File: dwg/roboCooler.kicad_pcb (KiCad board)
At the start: 2 copper layers, 61 x 78.7 mm, 66 parts, among them J1 CONN_01X02, J10 CONN_02X03, J11 CONN_01X04, J12 USB_A, J13 CONN_02X03, J14 CONN_02X03, J2 CONN_01X02, J3 Discovery_F407_P1, J4 CONN_01X06, J5 CONN_01X12, J6 Discovery_F407_P2, J7 CONN_02X03, J8 CONN_02X03, Q1 NMOS, Q2 NMOS, U1 SN74LV, U2 TB6549

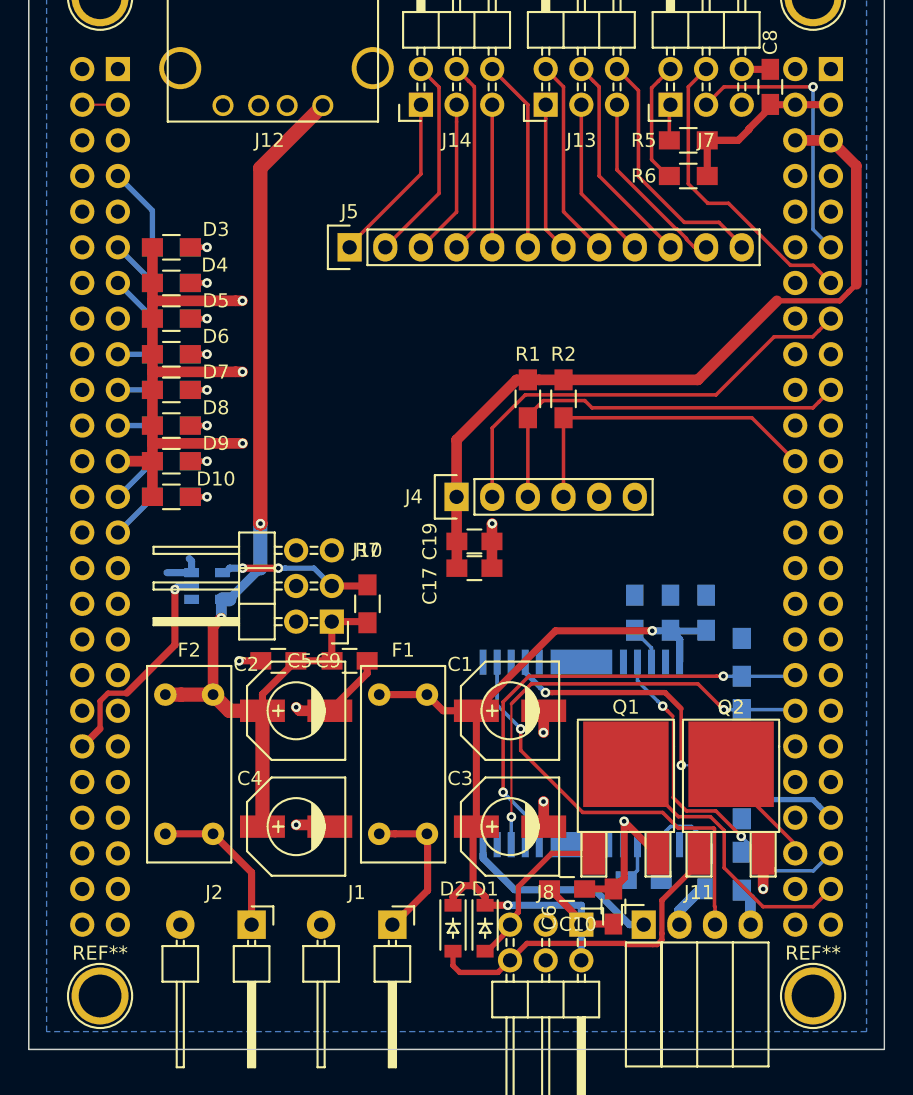
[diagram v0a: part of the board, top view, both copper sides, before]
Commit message: increased trace widths for led driver
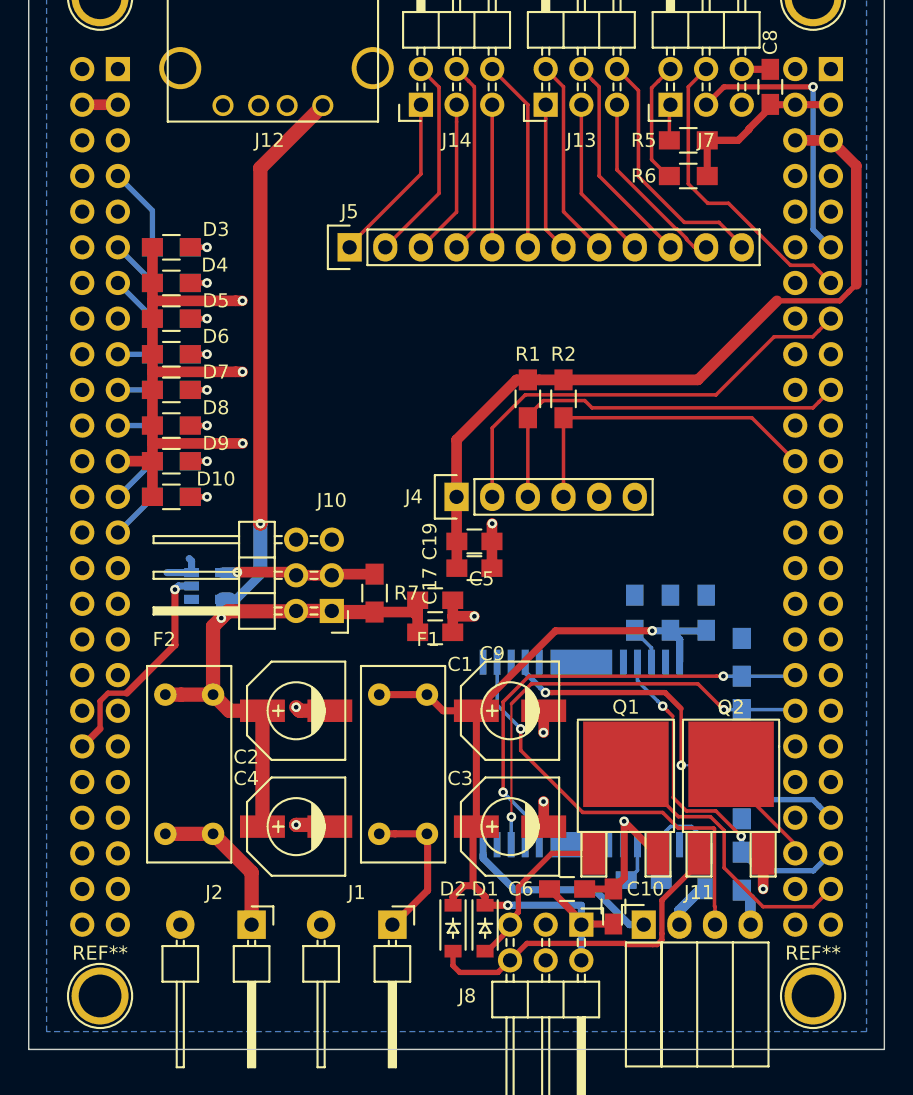
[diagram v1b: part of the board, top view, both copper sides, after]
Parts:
- moved C9 11.4 mm to (50.5, 65.5), turned to 0 degrees
- moved C5 7.47 mm to (50.5, 63.2)
- moved R7 0.92 mm to (46.2, 62.7)
- moved J10 0.76 mm to (43.2, 64.0)
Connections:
- J10 pad 2: (no net) -> +5V
- J10 pad 4: (no net) -> Net-(J10-Pad3)
- J10 pad 6: (no net) -> GND
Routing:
- net +5V: track 73.8 -> 78.6 mm
- net GND: track 81.5 -> 79.2 mm
- net MOTOR_SB: track 24.7 -> 25.3 mm
- net Net-(J10-Pad3): track 11.1 -> 11.0 mm, vias 2 -> 1

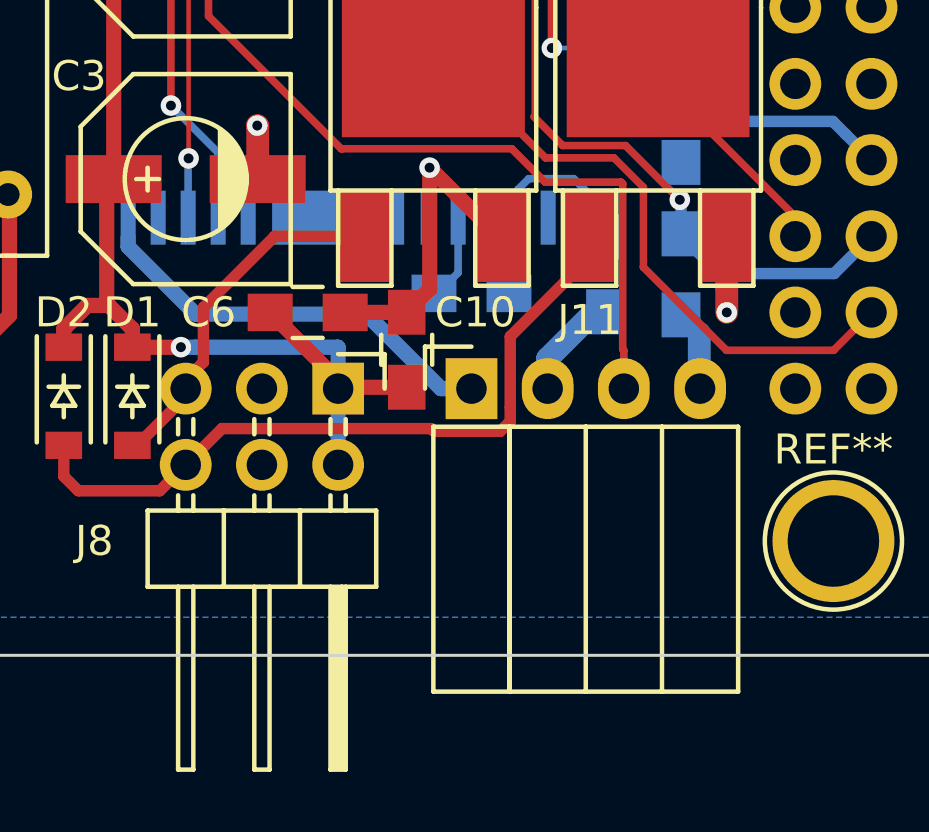
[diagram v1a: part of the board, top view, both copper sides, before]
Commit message: moved J11 to the same 6pin connector.
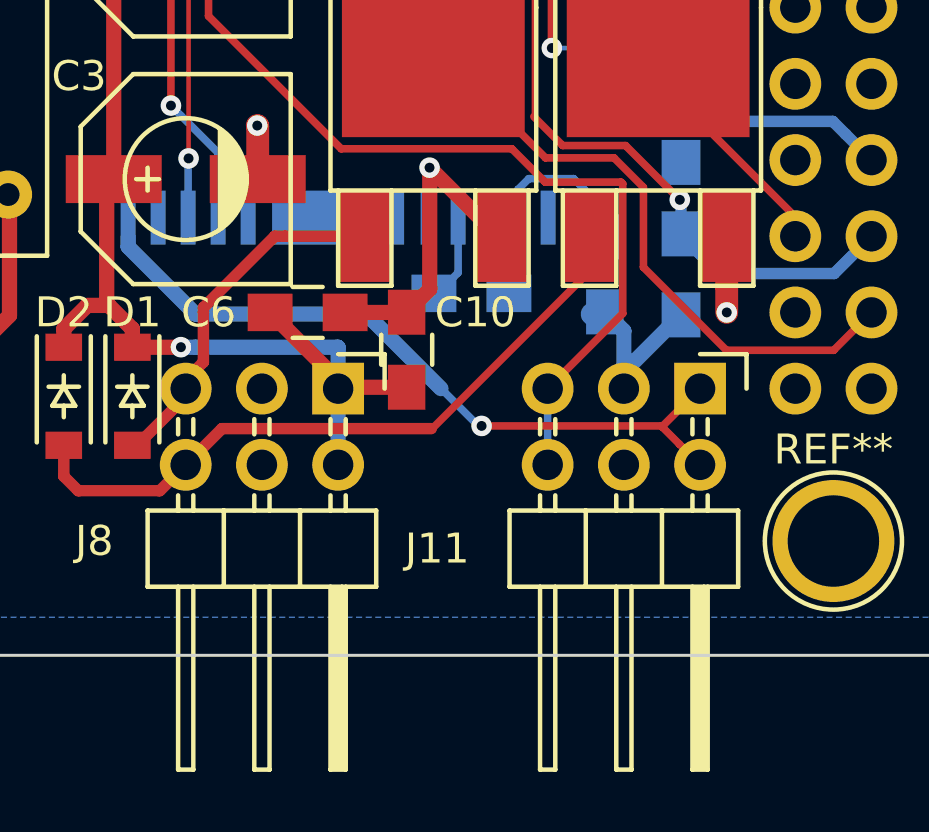
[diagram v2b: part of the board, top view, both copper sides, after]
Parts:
- J11: value CONN_01X04 -> CONN_02X03; footprint Socket_Strips:Socket_Strip_Angled_1x04 -> Pin_Headers:Pin_Header_Angled_2x03
- moved J11 7.62 mm to (73.0, 86.4), turned to 270 degrees
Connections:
- J11 pad 2: GND -> MOTOR_OUT1
- J11 pad 3: MOTOR_OUT2 -> GND
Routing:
- net MOTOR_OUT1: track 14.4 -> 24.9 mm, vias 0 -> 1
- net MOTOR_OUT2: track 30.1 -> 34.1 mm
- net Net-(D2-Pad2): track 24.8 -> 23.3 mm

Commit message: tweaked layout before ordering
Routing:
- net +12V: track 65.7 -> 64.9 mm

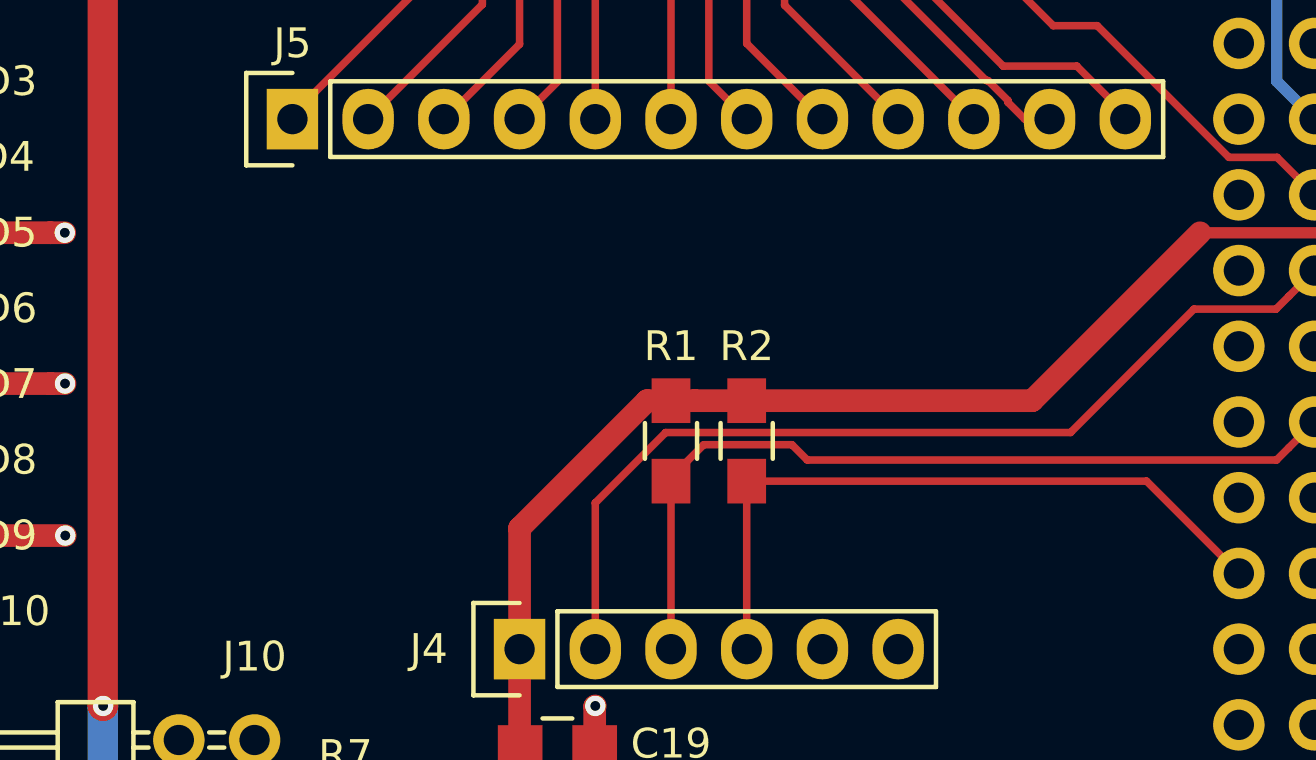
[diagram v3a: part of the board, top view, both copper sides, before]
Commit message: added board name, rev, & sn to silkscreen
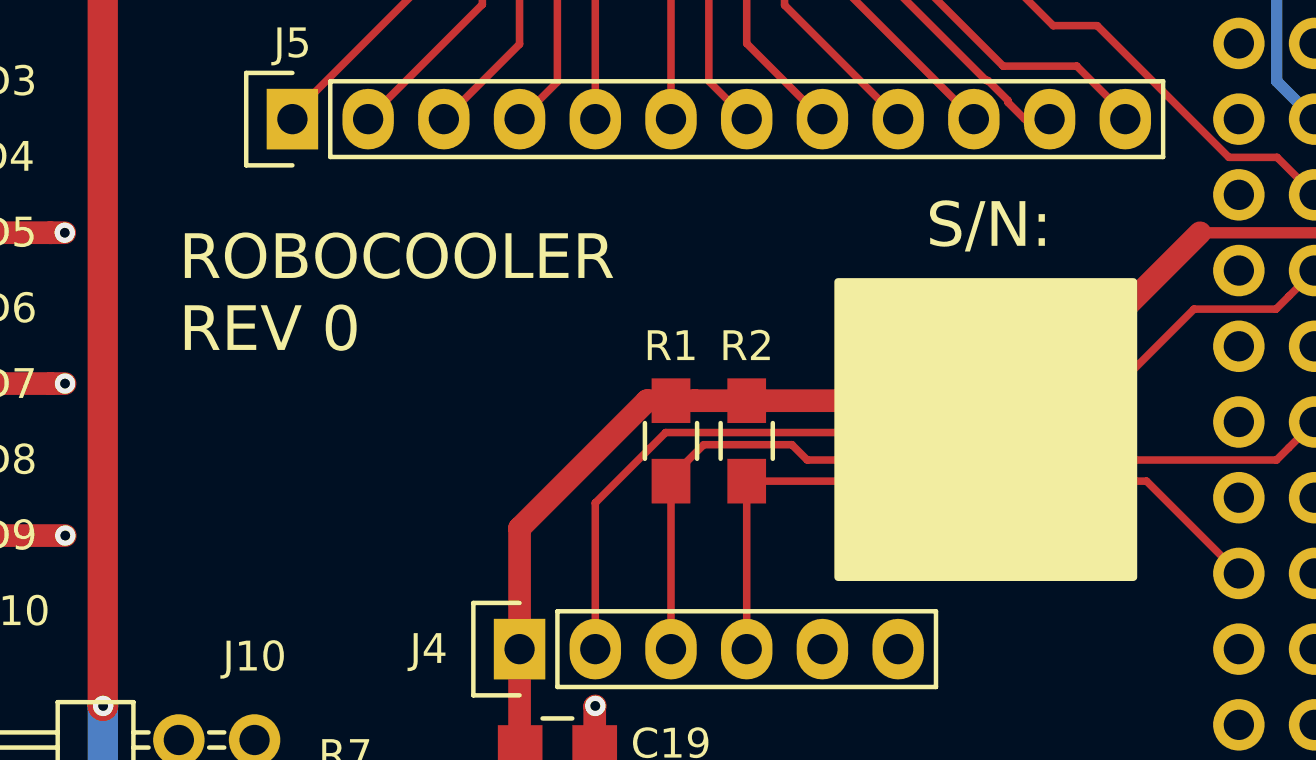
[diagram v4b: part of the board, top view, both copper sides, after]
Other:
- board text added: "ROBOCOOLER REV 0"
- board text added: "S/N:"
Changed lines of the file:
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@@
     (area 21.539999 16.459999 82.600001 95.300001)
     (thickness 1.6)
-    (drawings 4)
+    (drawings 6)
     (tracks 468)
     (zones 0)
@@
   (layers
     (0 F.Cu signal)
-    (31 B.Cu signal)
+    (31 B.Cu signal hide)
     (33 F.Adhes user)
     (35 F.Paste user)
@@
     )
   )
+  (gr_text "S/N: " (at 67.818 41.656) (layer F.SilkS)
+    (effects (font (size 1.5 1.5) (thickness 0.3)))
+  )
+  (gr_text "ROBOCOOLER\nREV 0" (at 40.64 43.942) (layer F.SilkS)
+    (effects (font (size 1.5 1.5) (thickness 0.3)) (justify left))
+  )
   (gr_line (start 21.59 95.25) (end 21.59 16.51) (layer Edge.Cuts) (width 0.1))
   (gr_line (start 82.55 95.25) (end 21.59 95.25) (layer Edge.Cuts) (width 0.1))
@@
       )
     )
+  )
+  (zone (net 0) (net_name "") (layer F.SilkS) (hatch full 0.508)
+    (connect_pads (clearance 0.508))
+    (min_thickness 0.254)
+    (fill yes (arc_segments 16) (thermal_gap 0.508) (thermal_bridge_width 0.508))
+    (polygon
+      (pts
+        (xy 62.629941 43.434) (xy 72.789941 43.434) (xy 72.789941 53.594) (xy 62.629941 53.594)
+      )
+    )

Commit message: updating board -- no DRC errors
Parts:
- removed J12: USB_A, Connect:USB_A
- removed J6: Discovery_F407_P2, roboCooler:Socket_Strip_Straight_2x25_Inverted
- removed REF** (x4): 1pin, Connect:1pin
- added C11: 2.2uF, Capacitors_SMD:C_0805_HandSoldering, B.Cu at (202.9, 87.1)
- added C12: 10uF, Capacitors_SMD:C_0805_HandSoldering, B.Cu at (194.1, 77.5)
- added C20: 2.2uF, Capacitors_SMD:C_0805_HandSoldering, B.Cu at (202.4, 79.5)
- added C21: 0.1uF, Capacitors_SMD:C_0805_HandSoldering, B.Cu at (184.4, 90.4)
- added C22: 0.1uF, Capacitors_SMD:C_0805_HandSoldering, B.Cu at (194.1, 81.5)
- added C23: 0.1uF, Capacitors_SMD:C_0805_HandSoldering, B.Cu at (194.1, 85.6)
- added C24: 0.1uF, Capacitors_SMD:C_0805_HandSoldering, B.Cu at (194.1, 89.7)
- added C25: 0.1uF, Capacitors_SMD:C_0805_HandSoldering, B.Cu at (205.5, 87.1)
- added C26: 0.1uF, Capacitors_SMD:C_0805_HandSoldering, B.Cu at (202.4, 77.5)
- added C27: 0.1uF, Capacitors_SMD:C_0805_HandSoldering, B.Cu at (194.1, 75.4)
- added C28: 20pF, Capacitors_SMD:C_0603_HandSoldering, F.Cu at (181.1, 78.7)
- added C29: 1uF, Capacitors_SMD:C_0805_HandSoldering, B.Cu at (194.1, 87.6)
- added C30: 20pF, Capacitors_SMD:C_0603_HandSoldering, F.Cu at (186.9, 78.7)
- added C31: 0.1uF, Capacitors_SMD:C_0805_HandSoldering, B.Cu at (194.1, 83.6)
- added C7: 0.1uF, Capacitors_SMD:C_0805_HandSoldering, B.Cu at (194.1, 79.5)
- added R18: 10k, Resistors_SMD:R_0805_HandSoldering, B.Cu at (198.4, 78.7)
- added R19: 10k, Resistors_SMD:R_0805_HandSoldering, B.Cu at (198.4, 87.1)
- added R20: 300, Resistors_SMD:R_0603_HandSoldering, F.Cu at (186.9, 84.8)
- added R21: 10k, Resistors_SMD:R_0805_HandSoldering, F.Cu at (222.0, 79.5)
- added SW1: TL3342, Buttons_Switches_SMD:SW_SPST_TL3342, F.Cu at (184.4, 90.4)
- added U3: STM32F407VGTx, Housings_QFP:LQFP-100_14x14mm_Pitch0.5mm, F.Cu at (198.4, 83.1)
- added Y1: 8MHz, Crystals:Crystal_SMD_Abracon_ABM3-2pin_5.0x3.2mm_HandSoldering, F.Cu at (183.9, 81.8)
- F1, F2: value 3568 -> PTC; footprint roboCooler:3568 -> Resistors_SMD:R_0603_HandSoldering
- J3: value Discovery_F407_P1 -> CONN_02X05; footprint roboCooler:Socket_Strip_Straight_2x25_Inverted -> Connectors:IDC_Header_Straight_10pins; moved to F.Cu
- R1, R2: footprint Resistors_SMD:R_0805_HandSoldering -> Resistors_SMD:R_0603_HandSoldering
- moved J3 203.3 mm to (218.7, 88.4), turned to 90 degrees
- moved D2 151.3 mm to (197.9, 126.2)
- moved D1 151.3 mm to (200.2, 126.2)
- moved J4 140.8 mm to (192.5, 66.0)
- moved C8 140.8 mm to (214.9, 36.8)
- moved J13 140.8 mm to (198.9, 38.1)
- moved J14 140.8 mm to (190.0, 38.1)
- moved J5 140.8 mm to (184.9, 48.3)
- moved J7 140.8 mm to (207.8, 38.1)
- moved R1 140.8 mm to (197.6, 59.1)
- moved R2 140.8 mm to (200.2, 59.1)
- moved R5 140.8 mm to (209.0, 40.6)
- moved R6 140.8 mm to (209.0, 43.2)
- moved J11 136.5 mm to (207.4, 110.5)
- moved J8 136.5 mm to (195.3, 110.5)
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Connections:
- J3 pad 1: GND -> VCC
- J3 pad 10: (no net) -> NRST
- J3 pad 2: GND -> JTMS/SWDIO
- J3 pad 3: VDD -> GND
- J3 pad 4: VDD -> JTCK/SWCLK
- J3 pad 6: (no net) -> JTDO/SWO
- J3 pad 7: LED_0 -> Net-(J3-Pad7)
- J3 pad 8: (no net) -> JTDI
- J3 pad 9: (no net) -> GND
- J4 pad 5: (no net) -> Net-(J4-Pad5)
- J8 pad 3: (no net) -> Net-(J8-Pad3)
- J8 pad 4: (no net) -> Net-(J8-Pad4)
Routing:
- net +5V: track 78.6 -> 5.48 mm, vias 2 -> 0
- net (no net): track 0.00 -> 70.1 mm, vias 0 -> 10
- net +12V: track 64.9 -> 0.00 mm, vias 2 -> 0
- net +3V3: track 55.8 -> 15.4 mm
- net MOTOR_OUT2: track 34.1 -> 0.00 mm, vias 1 -> 0
- net MOTOR_IN1: track 32.4 -> 0.00 mm, vias 2 -> 0
- net CS_IRQ: track 32.3 -> 0.00 mm
- net GND: track 79.6 -> 47.3 mm, vias 11 -> 4
- net MOTOR_IN2: track 31.7 -> 0.00 mm, vias 2 -> 0
- net MOTOR_PWM: track 29.2 -> 0.00 mm, vias 2 -> 0
- net MOTOR_SB: track 25.3 -> 0.00 mm, vias 2 -> 0
- net MOTOR_OUT1: track 24.9 -> 0.00 mm, vias 1 -> 0
- net Net-(D2-Pad2): track 23.3 -> 0.00 mm
- net CS_SCL: track 28.5 -> 5.76 mm
- net HALL_2: track 21.8 -> 0.00 mm
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- removed copper zone on B.Cu, net GND
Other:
- board outline removed
- board text added: "ROBOCOOLER REV 1"
- board text removed: "ROBOCOOLER REV 0"
